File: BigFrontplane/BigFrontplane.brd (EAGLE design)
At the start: 183.8 x 94.6 mm, 13 parts

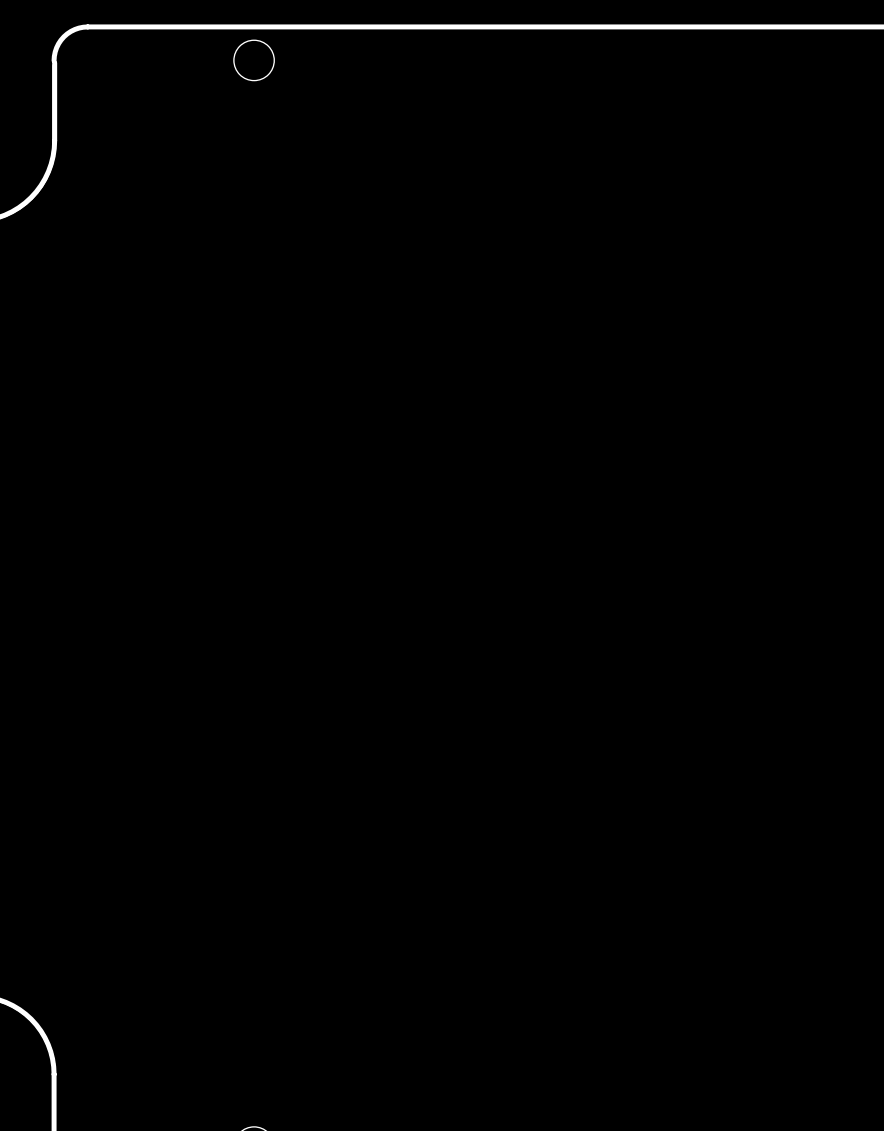
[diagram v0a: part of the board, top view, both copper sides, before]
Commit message: Updated Front Panel
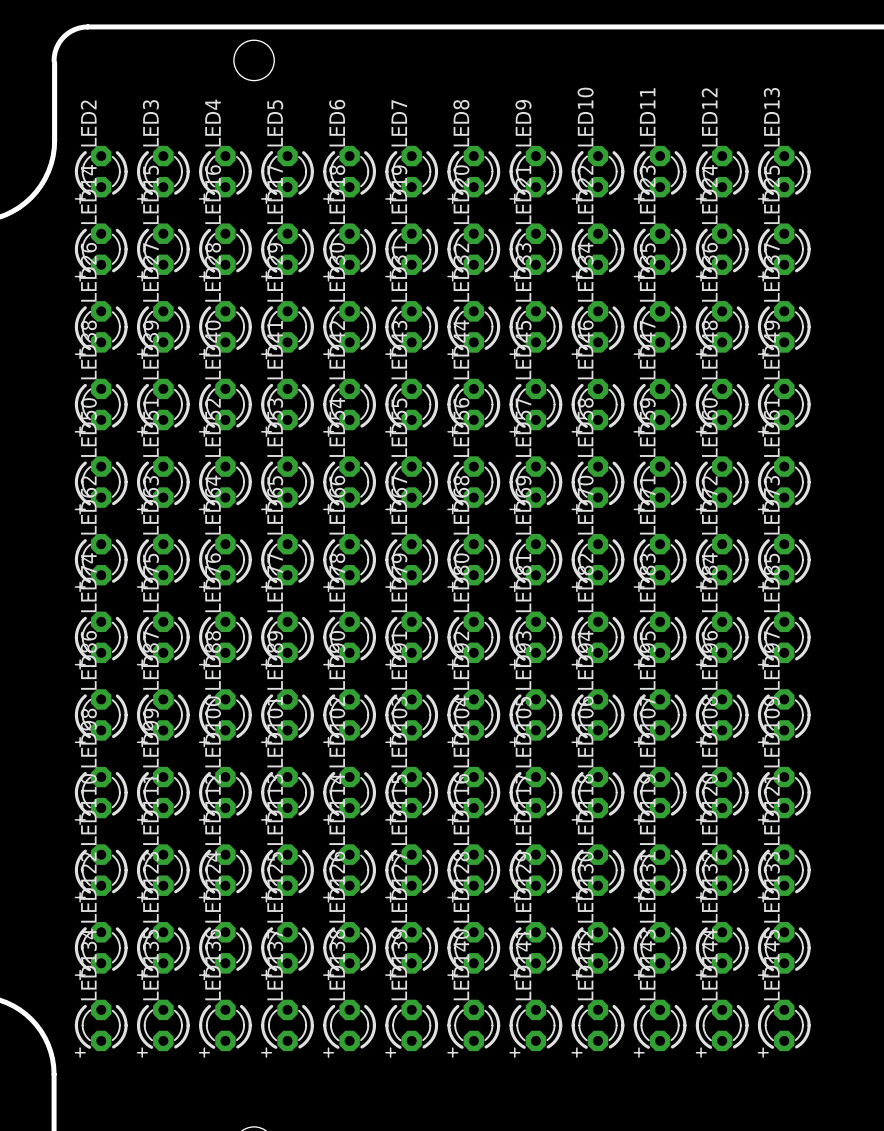
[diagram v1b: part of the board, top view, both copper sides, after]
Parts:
- added LED10, LED100, LED101, LED102, LED103, LED104, LED105, LED106, LED107, LED108, LED109, LED11, LED110, LED111, LED112, LED113, LED114, LED115, LED116, LED117, LED118, LED119, LED12, LED120, LED121, LED122, LED123, LED124, LED125, LED126, LED127, LED128, LED129, LED13, LED130, LED131, LED132, LED133, LED134, LED135, LED136, LED137, LED138, LED139, LED14, LED140, LED141, LED142, LED143, LED144, LED145, LED15, LED16, LED17, LED18, LED19, LED2, LED20, LED21, LED22, LED23, LED24, LED25, LED26, LED27, LED28, LED29, LED3, LED30, LED31, LED32, LED33, LED34, LED35, LED36, LED37, LED38, LED39, LED4, LED40, LED41, LED42, LED43, LED44, LED45, LED46, LED47, LED48, LED49, LED5, LED50, LED51, LED52, LED53, LED54, LED55, LED56, LED57, LED58, LED59, LED6, LED60, LED61, LED62, LED63, LED64, LED65, LED66, LED67, LED68, LED69, LED7, LED70, LED71, LED72, LED73, LED74, LED75, LED76, LED77, LED78, LED79, LED8, LED80, LED81, LED82, LED83, LED84, LED85, LED86, LED87, LED88, LED89, LED9, LED90, LED91, LED92, LED93, LED94, LED95, LED96, LED97, LED98, LED99: (no value), adafruit:LED3MM
